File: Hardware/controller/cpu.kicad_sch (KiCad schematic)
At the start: 41 parts, among them J301 Conn_ARM_JTAG_SWD_10, J302 Conn_01x03_Male, Q301 MMBT3904, SW301 B3F-1005, SW302 B3F-1002, SW303 228ADS2AAWFCMBA, U302 ATSAME51J20A-A, U303 AT25SF321B-SSHB, Y301 32.768kHz, Y302 12MHz

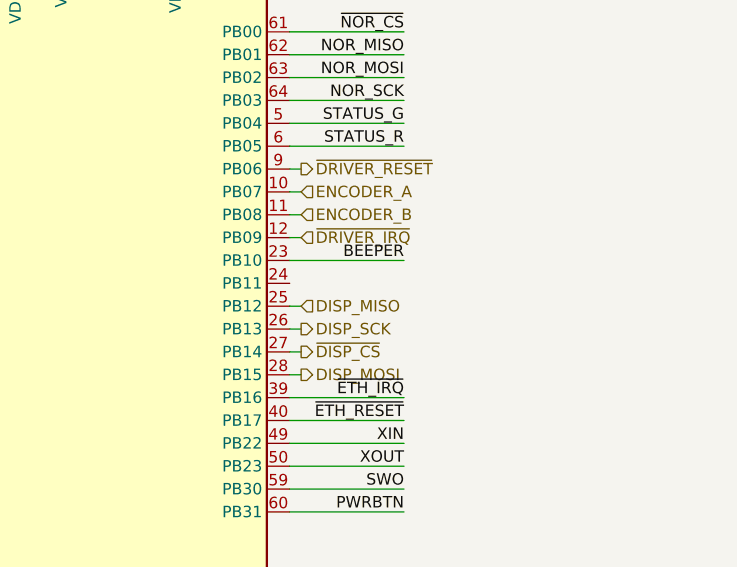
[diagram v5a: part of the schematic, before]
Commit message: External trigger input
- Added a basic Schmitt-trigger based external trigger input. There's a
  basic pulse shaping circuit attached to it, before its fed into the
  buffer, and then off to the main board to use as an interrupt line to
  control the system mode.
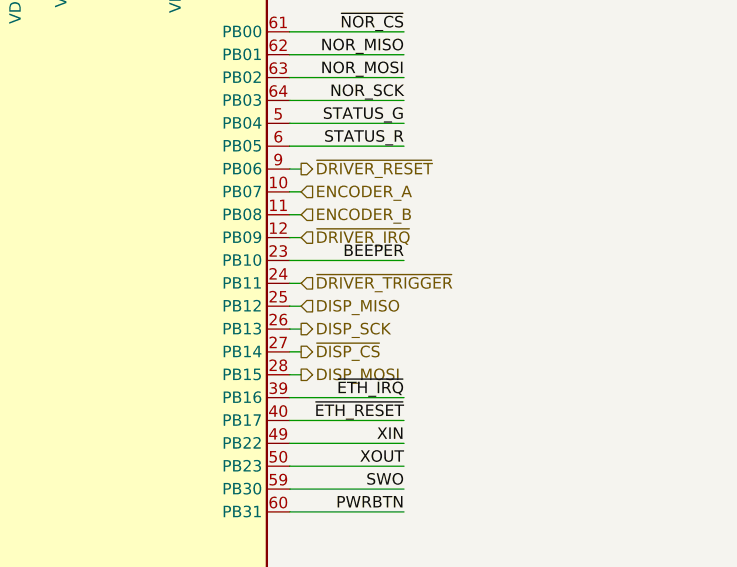
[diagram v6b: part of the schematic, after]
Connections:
- net ~{DRIVER_TRIGGER}: now reaches U302.24 (PB11)
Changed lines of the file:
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@@
+    (stroke (width 0) (type default) (color 0 0 0 0))
+  )
+  (wire (pts (xy 234.315 76.2) (xy 235.585 76.2))
     (stroke (width 0) (type default) (color 0 0 0 0))
   )
@@
     (effects (font (size 1.27 1.27)) (justify right))
   )
+  (hierarchical_label "~{DRIVER_TRIGGER}" (shape input) (at 235.585 76.2 0)
+    (effects (font (size 1.27 1.27)) (justify left))
+  )
   (symbol (lib_id "power:GND") (at 138.43 163.195 0) (unit 1)

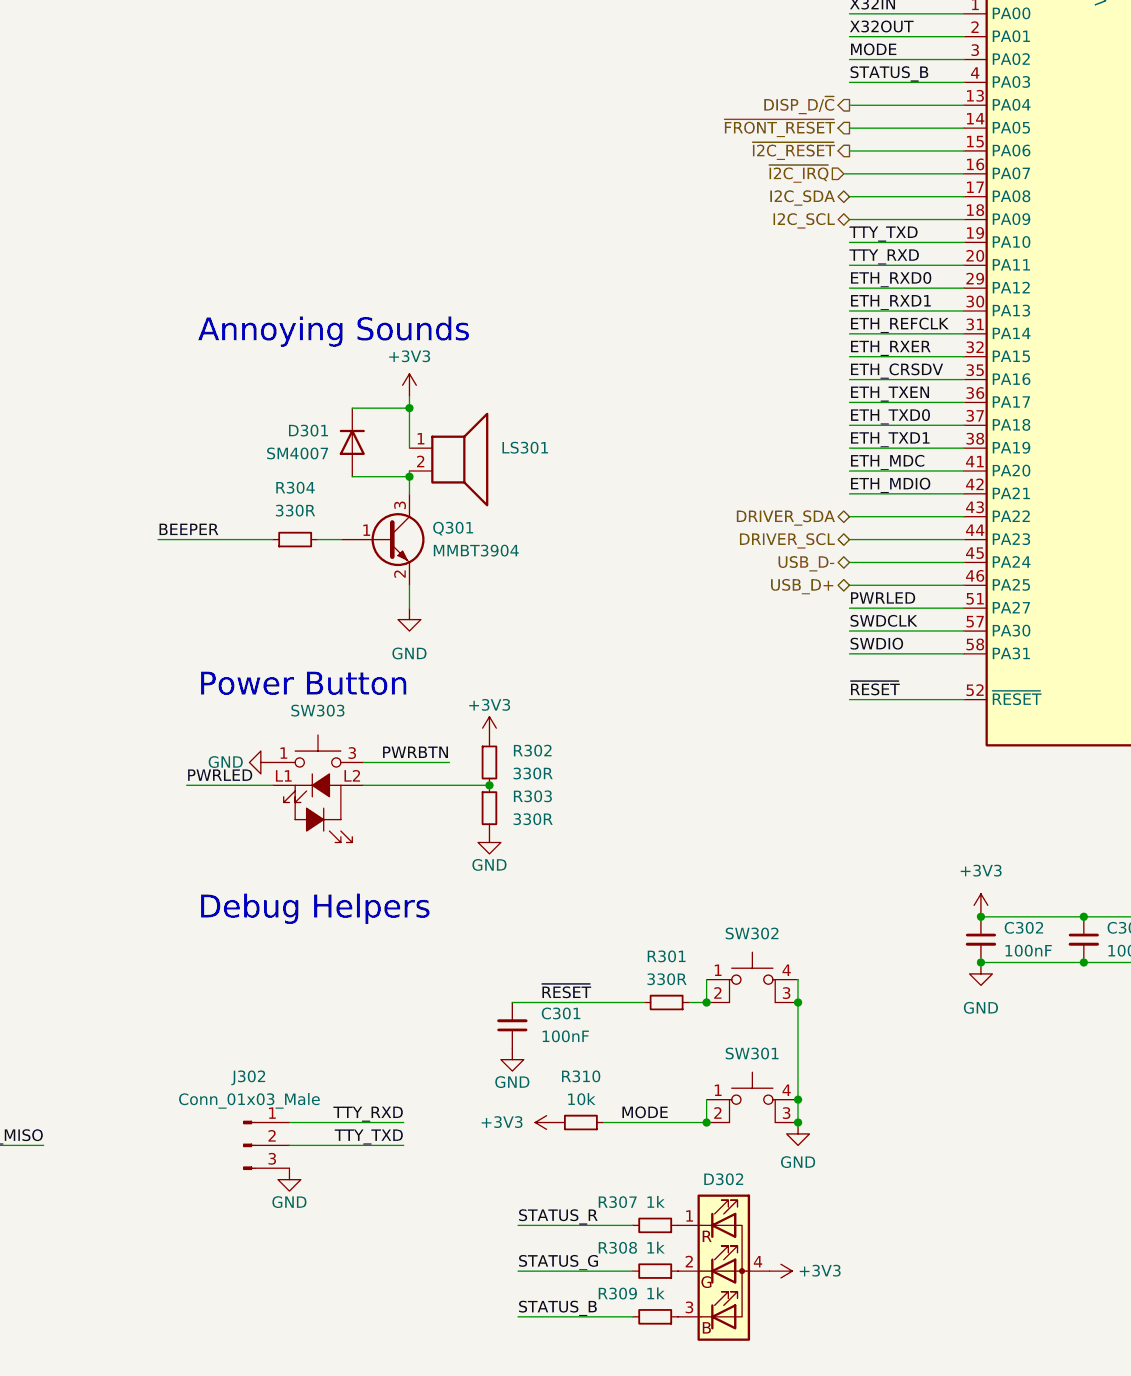
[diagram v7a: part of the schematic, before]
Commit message: Reworked /I2C_IRQ line
- Moved the /I2C_IRQ signal to PA10 so that it no longer conflicts with
  the external interrupt (EIC) input line for the encoder at PB07.

- Remove the superfluous UART header, as we're not actually going to use
  the UART for anything. This will all take place over USB CDC instead,
  and use SWD for early boot output.
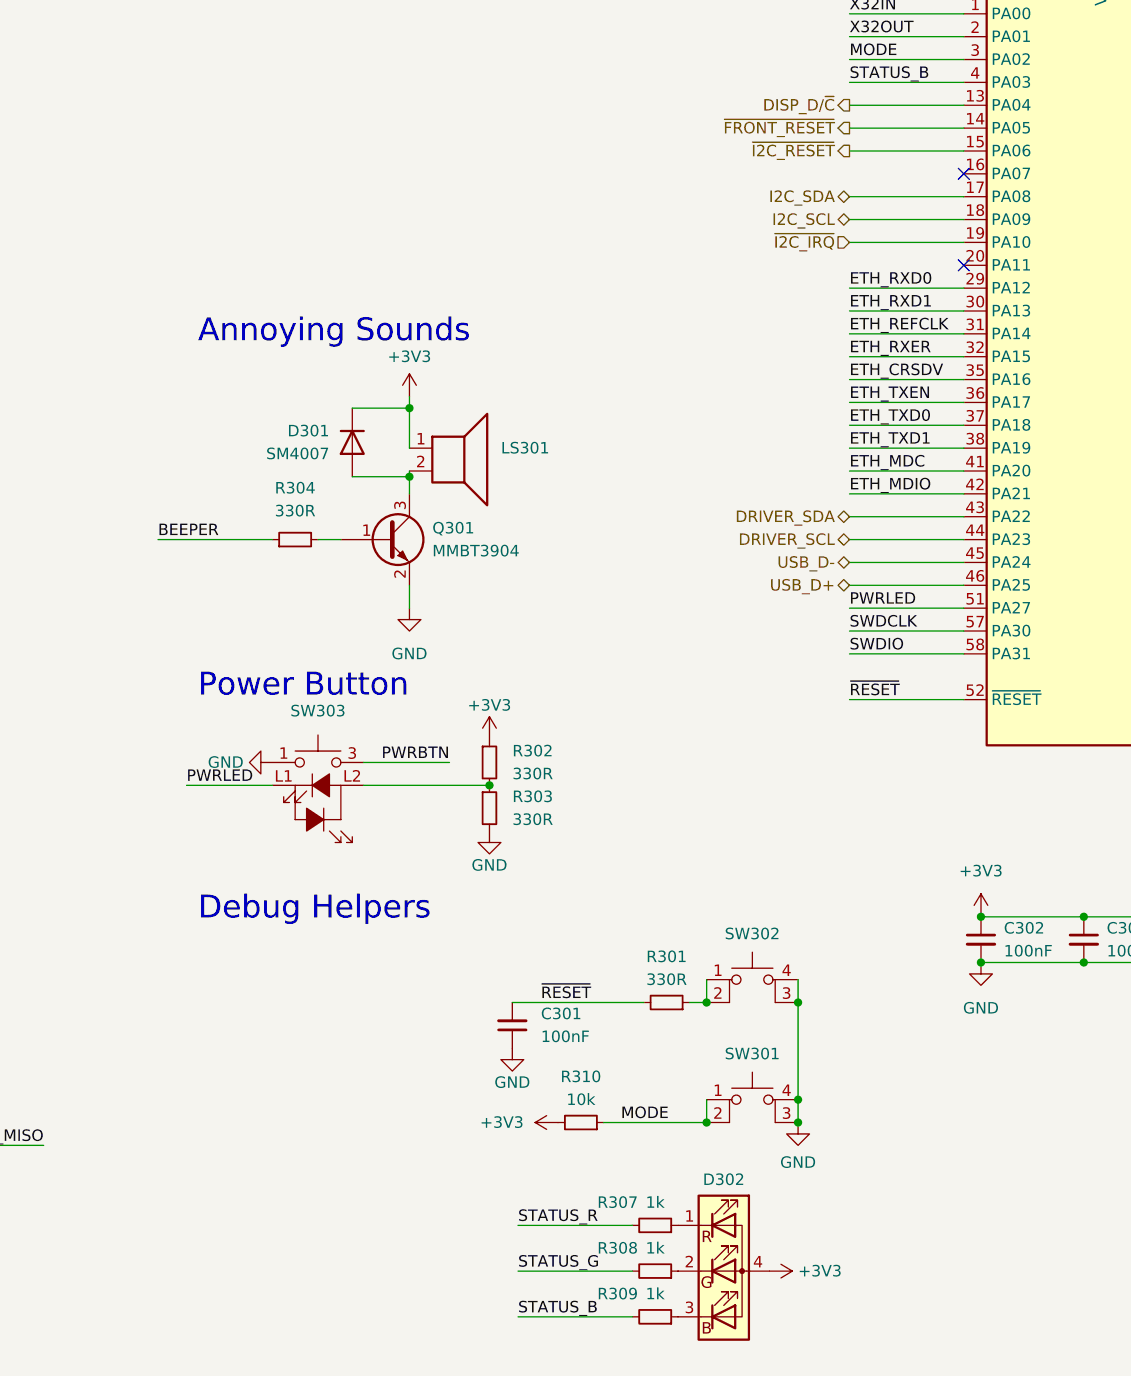
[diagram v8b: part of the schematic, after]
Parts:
- removed J302: Conn_01x03_Male, Connector_PinHeader_2.54mm:PinHeader_1x03_P2.54mm_Vertical, symbol Connector:Conn_01x03_Male
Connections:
- net TTY_TXD is gone; now on net ~{I2C_IRQ}: U302.19 (PA10)
- net ~{I2C_IRQ}: no longer U302.16 (PA07)
- net TTY_RXD: no longer names the net of U302.20 (PA11)
- no-connect marks 0 -> 2
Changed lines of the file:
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@@
   (title_block
     (title "Processor Complex")
-    (date "2022-03-06")
-    (rev "1")
+    (date "2022-03-20")
+    (rev "2")
     (comment 1 "For Ethernet, substitute U302 with SAME53J20")
   )
@@
   (junction (at 201.93 153.67) (diameter 0) (color 0 0 0 0)
   )
+  (no_connect (at 188.595 76.2))
+  (no_connect (at 188.595 66.04))
   (wire (pts (xy 38.1 123.825) (xy 39.37 123.825))
     (stroke (width 0) (type default) (color 0 0 0 0))
@@
     (stroke (width 0) (type default) (color 0 0 0 0))
   )
-  (wire (pts (xy 126.365 171.45) (xy 113.665 171.45))
-    (stroke (width 0) (type default) (color 0 0 0 0))
-  )
   (wire (pts (xy 19.05 30.48) (xy 19.05 46.99))
     (stroke (width 0) (type default) (color 0 0 0 0))
@@
     (stroke (width 0) (type default) (color 0 0 0 0))
   )
-  (wire (pts (xy 126.365 173.99) (xy 113.665 173.99))
-    (stroke (width 0) (type default) (color 0 0 0 0))
-  )
   (wire (pts (xy 246.38 146.05) (xy 255.905 146.05))
     (stroke (width 0) (type default) (color 0 0 0 0))
@@
     (stroke (width 0) (type default) (color 0 0 0 0))
   )
-  (wire (pts (xy 175.26 66.04) (xy 188.595 66.04))
-    (stroke (width 0) (type default) (color 0 0 0 0))
-  )
   (wire (pts (xy 190.5 148.59) (xy 201.93 148.59))
     (stroke (width 0) (type default) (color 0 0 0 0))
@@
   )
   (wire (pts (xy 151.765 182.88) (xy 139.065 182.88))
-    (stroke (width 0) (type default) (color 0 0 0 0))
-  )
-  (wire (pts (xy 175.895 76.2) (xy 188.595 76.2))
     (stroke (width 0) (type default) (color 0 0 0 0))
   )
@@
     (effects (font (size 1.27 1.27)) (justify right bottom))
   )
-  (label "TTY_RXD" (at 126.365 171.45 180)
-    (effects (font (size 1.27 1.27)) (justify right bottom))
-  )
   (label "ETH_TXD0" (at 175.895 93.98 0)
     (effects (font (size 1.27 1.27)) (justify left bottom))
@@
     (effects (font (size 1.27 1.27)) (justify right bottom))
   )
-  (label "TTY_TXD" (at 175.895 73.66 0)
-    (effects (font (size 1.27 1.27)) (justify left bottom))
-  )
   (label "STATUS_R" (at 139.065 182.88 0)
     (effects (font (size 1.27 1.27)) (justify left bottom))
@@
     (effects (font (size 1.27 1.27)) (justify right bottom))
   )
-  (label "TTY_TXD" (at 126.365 173.99 180)
-    (effects (font (size 1.27 1.27)) (justify right bottom))
-  )
   (label "XIN" (at 247.015 93.98 180)
     (effects (font (size 1.27 1.27)) (justify right bottom))
@@
   )
   (label "ETH_MDC" (at 175.895 99.06 0)
-    (effects (font (size 1.27 1.27)) (justify left bottom))
-  )
-  (label "TTY_RXD" (at 175.895 76.2 0)
     (effects (font (size 1.27 1.27)) (justify left bottom))
   )
@@
     (effects (font (size 1.27 1.27)) (justify right))
   )
-  (hierarchical_label "~{I2C_IRQ}" (shape input) (at 175.26 66.04 180)
+  (hierarchical_label "~{I2C_IRQ}" (shape input) (at 175.895 73.66 180)
     (effects (font (size 1.27 1.27)) (justify right))
   )
@@
     (pin "1")
     (pin "2")
-  )
-  (symbol (lib_id "power:GND") (at 113.665 176.53 0) (unit 1)
-    (in_bom yes) (on_board yes)
-    (property "Reference" "#PWR0328" (id 0) (at 113.665 182.88 0)
-      (effects (font (size 1.27 1.27)) hide)
-    )
-    (property "Value" "GND" (id 1) (at 113.665 180.34 0))
-    (property "Footprint" "" (id 2) (at 113.665 176.53 0)
-      (effects (font (size 1.27 1.27)) hide)
-    )
-    (property "Datasheet" "" (id 3) (at 113.665 176.53 0)
-      (effects (font (size 1.27 1.27)) hide)
-    )
-    (pin "1")
   )
   (symbol (lib_id "power:+3V3") (at 208.915 35.56 0) (unit 1)
@@
     (pin "2")
   )
-  (symbol (lib_id "Connector:Conn_01x03_Male") (at 108.585 173.99 0) (unit 1)
-    (in_bom yes) (on_board yes) (fields_autoplaced)
-    (property "Reference" "J302" (id 0) (at 109.22 166.37 0))
-    (property "Value" "Conn_01x03_Male" (id 1) (at 109.22 168.91 0))
-    (property "Footprint" "Connector_PinHeader_2.54mm:PinHeader_1x03_P2.54mm_Vertical" (id 2) (at 108.585 173.99 0)
-      (effects (font (size 1.27 1.27)) hide)
-    )
-    (property "Datasheet" "~" (id 3) (at 108.585 173.99 0)
-      (effects (font (size 1.27 1.27)) hide)
-    )
-    (pin "1")
-    (pin "2")
-    (pin "3")
-  )
   (symbol (lib_id "power:+3V3") (at 135.89 128.905 0) (unit 1)
